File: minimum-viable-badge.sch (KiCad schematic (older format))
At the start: 42 parts, among them P1 BATTERY, P10 POT_4, P11 MECH, P12 MECH, P13 MECH, P2 USB, P3 CONN_01X14, P4 eInk, P5 CONN_01X10, P6 POT_1, P7 POT_2, P8 CONN_01X14, P9 POT_3, Q1 S8050, Q2 S8050, SW1 PRGM, SW2 RESET, U1 CP2102, U2 ESP32-WROOM

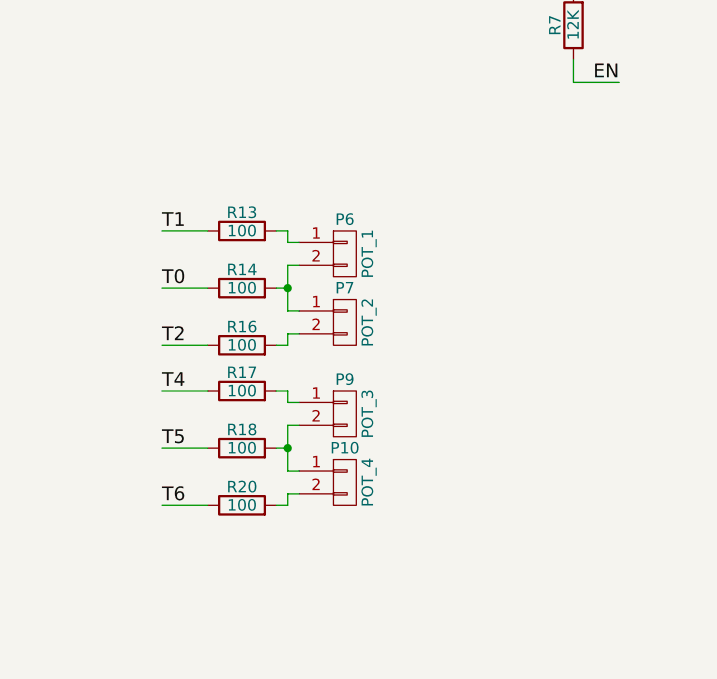
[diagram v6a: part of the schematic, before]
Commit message: updated touch sensors
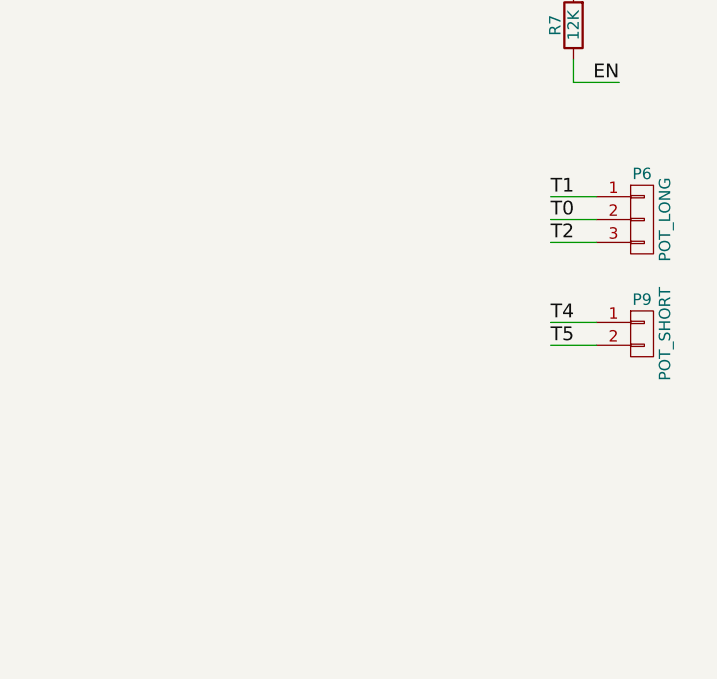
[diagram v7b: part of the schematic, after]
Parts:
- removed P10: POT_4, libs:sense_pot, symbol CONN_01X02
- removed P6: POT_1, libs:sense_pot, symbol CONN_01X02
- removed P7: POT_2, libs:sense_pot, symbol CONN_01X02
- removed R13, R14, R16, R17, R18, R20: 100, Resistors_SMD:R_0603_HandSoldering, symbol R
- added P6: POT_LONG, libs:sense_long, symbol CONN_01X03
- P9: value POT_3 -> POT_SHORT; footprint libs:sense_pot -> libs:sense_short
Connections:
- net IO12: now also P6.1 (P1)
- net IO13: now also P6.3 (P3)
- net IO14: now also P6.2 (P2)
- net IO15: now also P9.1 (P1)
- net IO2: now also P9.2 (P2)
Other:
- moved on the sheet: P9
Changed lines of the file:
@@
 	-1   0    0    1
 $EndComp
-Text Label 8700 5000 0    60   ~ 0
+Text Label 10400 4550 0    60   ~ 0
 T2
-Text Label 8700 5200 0    60   ~ 0
+Text Label 10400 4900 0    60   ~ 0
 T4
-Text Label 8700 5450 0    60   ~ 0
+Text Label 10400 5000 0    60   ~ 0
 T5
-Text Label 8700 5700 0    60   ~ 0
-T6
 Text Label 5750 2300 0    60   ~ 0
 CS
@@
 NoConn ~ 6150 6350
 NoConn ~ 6150 6450
-$Comp
-L CONN_01X02 P7
-U 1 1 5936BA63
-P 9500 4900
-F 0 "P7" H 9500 5050 50  0000 C CNN
-F 1 "POT_2" V 9600 4900 50  0000 C CNN
-F 2 "libs:sense_pot" H 9500 4900 50  0001 C CNN
-F 3 "" H 9500 4900 50  0000 C CNN
-	1    9500 4900
-	1    0    0    -1
-$EndComp
-$Comp
-L R R16
-U 1 1 5936C5EF
-P 9050 5000
-F 0 "R16" V 9130 5000 50  0000 C CNN
-F 1 "100" V 9050 5000 50  0000 C CNN
-F 2 "Resistors_SMD:R_0603_HandSoldering" V 8980 5000 50  0001 C CNN
-F 3 "" H 9050 5000 50  0000 C CNN
-	1    9050 5000
-	0    -1   -1   0
-$EndComp
 Wire Wire Line
-	8700 5000 8900 5000
-Wire Wire Line
-	9250 4850 9300 4850
-Wire Wire Line
-	9200 5000 9250 5000
-Wire Wire Line
-	9250 5000 9250 4950
-Wire Wire Line
-	9250 4950 9300 4950
+	10400 4550 10600 4550
 Text Label 5750 2500 0    60   ~ 0
 T1
-Text Label 8700 4750 0    60   ~ 0
+Text Label 10400 4450 0    60   ~ 0
 T0
-Text Label 8700 4500 0    60   ~ 0
+Text Label 10400 4350 0    60   ~ 0
 T1
-$Comp
-L CONN_01X02 P6
-U 1 1 5936FB83
-P 9500 4600
-F 0 "P6" H 9500 4750 50  0000 C CNN
-F 1 "POT_1" V 9600 4600 50  0000 C CNN
-F 2 "libs:sense_pot" H 9500 4600 50  0001 C CNN
-F 3 "" H 9500 4600 50  0000 C CNN
-	1    9500 4600
-	1    0    0    -1
-$EndComp
-$Comp
-L R R14
-U 1 1 5936FB89
-P 9050 4750
-F 0 "R14" V 9130 4750 50  0000 C CNN
-F 1 "100" V 9050 4750 50  0000 C CNN
-F 2 "Resistors_SMD:R_0603_HandSoldering" V 8980 4750 50  0001 C CNN
-F 3 "" H 9050 4750 50  0000 C CNN
-	1    9050 4750
-	0    -1   -1   0
-$EndComp
-$Comp
-L R R13
-U 1 1 5936FB8F
-P 9050 4500
-F 0 "R13" V 9130 4500 50  0000 C CNN
-F 1 "100" V 9050 4500 50  0000 C CNN
-F 2 "Resistors_SMD:R_0603_HandSoldering" V 8980 4500 50  0001 C CNN
-F 3 "" H 9050 4500 50  0000 C CNN
-	1    9050 4500
-	0    -1   -1   0
-$EndComp
 Wire Wire Line
-	8700 4500 8900 4500
+	10400 4350 10600 4350
 Wire Wire Line
-	8700 4750 8900 4750
-Wire Wire Line
-	9200 4500 9250 4500
-Wire Wire Line
-	9250 4500 9250 4550
-Wire Wire Line
-	9250 4550 9300 4550
-Wire Wire Line
-	9250 4650 9300 4650
-$Comp
-L CONN_01X02 P10
-U 1 1 5937167F
-P 9500 5600
-F 0 "P10" H 9500 5750 50  0000 C CNN
-F 1 "POT_4" V 9600 5600 50  0000 C CNN
-F 2 "libs:sense_pot" H 9500 5600 50  0001 C CNN
-F 3 "" H 9500 5600 50  0000 C CNN
-	1    9500 5600
-	1    0    0    -1
-$EndComp
-$Comp
-L R R20
-U 1 1 59371685
-P 9050 5700
-F 0 "R20" V 9130 5700 50  0000 C CNN
-F 1 "100" V 9050 5700 50  0000 C CNN
-F 2 "Resistors_SMD:R_0603_HandSoldering" V 8980 5700 50  0001 C CNN
-F 3 "" H 9050 5700 50  0000 C CNN
-	1    9050 5700
-	0    -1   -1   0
-$EndComp
-Wire Wire Line
-	8700 5700 8900 5700
-Wire Wire Line
-	9250 5550 9300 5550
-Wire Wire Line
-	9200 5700 9250 5700
-Wire Wire Line
-	9250 5700 9250 5650
-Wire Wire Line
-	9250 5650 9300 5650
+	10400 4450 10600 4450
 $Comp
 L CONN_01X02 P9
 U 1 1 5937169B
-P 9500 5300
-F 0 "P9" H 9500 5450 50  0000 C CNN
-F 1 "POT_3" V 9600 5300 50  0000 C CNN
-F 2 "libs:sense_pot" H 9500 5300 50  0001 C CNN
-F 3 "" H 9500 5300 50  0000 C CNN
-	1    9500 5300
+P 10800 4950
+F 0 "P9" H 10800 5100 50  0000 C CNN
+F 1 "POT_SHORT" V 10900 4950 50  0000 C CNN
+F 2 "libs:sense_short" H 10800 4950 50  0001 C CNN
+F 3 "" H 10800 4950 50  0000 C CNN
+	1    10800 4950
 	1    0    0    -1
 $EndComp
-$Comp
-L R R18
-U 1 1 593716A1
-P 9050 5450
-F 0 "R18" V 9130 5450 50  0000 C CNN
-F 1 "100" V 9050 5450 50  0000 C CNN
-F 2 "Resistors_SMD:R_0603_HandSoldering" V 8980 5450 50  0001 C CNN
-F 3 "" H 9050 5450 50  0000 C CNN
-	1    9050 5450
-	0    -1   -1   0
-$EndComp
-$Comp
-L R R17
-U 1 1 593716A7
-P 9050 5200
-F 0 "R17" V 9130 5200 50  0000 C CNN
-F 1 "100" V 9050 5200 50  0000 C CNN
-F 2 "Resistors_SMD:R_0603_HandSoldering" V 8980 5200 50  0001 C CNN
-F 3 "" H 9050 5200 50  0000 C CNN
-	1    9050 5200
-	0    -1   -1   0
-$EndComp
 Wire Wire Line
-	8700 5200 8900 5200
+	10400 4900 10600 4900
 Wire Wire Line
-	8700 5450 8900 5450
-Wire Wire Line
-	9200 5200 9250 5200
-Wire Wire Line
-	9250 5200 9250 5250
-Wire Wire Line
-	9250 5250 9300 5250
-Wire Wire Line
-	9250 5350 9300 5350
-Wire Wire Line
-	9250 4650 9250 4850
-Wire Wire Line
-	9250 4750 9200 4750
-Connection ~ 9250 4750
-Wire Wire Line
-	9250 5350 9250 5550
-Wire Wire Line
-	9250 5450 9200 5450
-Connection ~ 9250 5450
+	10400 5000 10600 5000
 $Comp
 L CONN_01X01 P13
@@
 	1    0    0    1
 $EndComp
+$Comp
+L CONN_01X03 P6
+U 1 1 59A0383A
+P 10800 4450
+F 0 "P6" H 10800 4650 50  0000 C CNN
+F 1 "POT_LONG" V 10900 4450 50  0000 C CNN
+F 2 "libs:sense_long" H 10800 4450 50  0001 C CNN
+F 3 "" H 10800 4450 50  0000 C CNN
+	1    10800 4450
+	1    0    0    -1
+$EndComp
 $EndSCHEMATC

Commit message: Added eInk decoupling caps.
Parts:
- added C? (x8): 1uF, Capacitors_SMD:C_0603_HandSoldering, symbol C
- added R?: 0R, Resistors_SMD:R_0603_HandSoldering, symbol R
- P2: symbol USB_OTG -> USB_OTG-RESCUE-minimum-viable-badge
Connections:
- net +3V3: now also P4.10 (P10), P4.9 (P9), R?.1; no longer P4.15 (P15), P4.16 (P16)
- net GND: now also P4.8 (P8), C?.1, C?.1, C?.1, C?.2, C?.2, C?.2, C?.2, C?.2; no longer P4.17 (P17)
- net I2C_SCL: now also P3.3 (P3), U2.12 (IO27); no longer P8.3 (P3), U2.36 (IO22)
- net I2C_SDA: now also P3.4 (P4), U2.11 (IO26); no longer P8.6 (P6), U2.33 (IO21)
- net IO18: now also P4.12 (P12)
- net IO19: now also P4.13 (P13)
- net IO23: now also P4.15 (P15)
- net IO32: no longer P4.14 (P14)
- net IO33: no longer P4.13 (P13)
- net IO5: now also P4.11 (P11)
- net VCOM: now reaches P4.1 (P1)
- net VCOM: now also C?.1
- net TSDA: now reaches P4.18 (P18)
- net TSCL: now reaches P4.19 (P19)
- net PREVGL: now reaches P4.2 (P2)
- net VGH: now reaches P4.20 (P20)
- net VGH: now also C?.1
- net VGL: now reaches P4.21 (P21)
- net VGL: now also C?.1
- net RESE: now reaches P4.22 (P22)
- net GDR: now reaches P4.23 (P23)
- net VSL: now reaches P4.3 (P3)
- net VSL: now also C?.1
- net PREVGH: now reaches P4.4 (P4)
- net VSH: now reaches P4.5 (P5)
- net VSH: now also C?.1
- net VPP: now reaches P4.6 (P6)
- net LCD_VDD: now reaches P4.7 (P7)
- net LCD_VDD: now also C?.2, R?.2
- removed net CS: P3.3 (P3), P4.10 (P10), U2.12 (IO27)
- net D/C renamed IO25
- net IO25: no longer P4.12 (P12)
- removed net IO26: P3.4 (P4), P4.11 (P11), U2.11 (IO26)
- new net IO21: P4.14 (P14), P8.6 (P6), U2.33 (IO21)
- new net IO22: P4.16 (P16), P8.3 (P3), U2.36 (IO22)
- no-connect marks 23 -> 8
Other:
- moved on the sheet: P4
